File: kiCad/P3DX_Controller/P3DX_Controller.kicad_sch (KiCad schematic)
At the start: 19 parts, among them J1 Conn_01x10_Pin, J2 Conn_01x26_Pin, J3 Conn_01x10_Pin, J4 Conn_01x16_Pin, J5 Conn_01x03_Pin, J6 Conn_01x05_Pin, U1 TXS0108EPW, U3 ESP32-DevKitC

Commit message: 20251202
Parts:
- removed R5: DO NOT PLACE, Resistor_THT:R_Axial_DIN0204_L3.6mm_D1.6mm_P7.62mm_Horizontal, symbol Device:R
- removed U4: ~, p3dx:MPU6050, symbol p3dx:MPU6050
- added J6: Conn_01x03_Pin, Connector_PinHeader_2.54mm:PinHeader_1x03_P2.54mm_Vertical, symbol Connector:Conn_01x03_Pin
- added R4: DO NOT PLACE, Resistor_THT:R_Axial_DIN0204_L3.6mm_D1.6mm_P7.62mm_Horizontal, symbol Device:R
- renumbered C3 to C1, C4 to C2, J6 to J7, R4 to R1, R1 to R2, R2 to R5, U3 to U2, U2 to U3
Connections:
- net i2c-scl is gone; now on net L_ENCODER_A_LV: U2.36 (GPIO22)
- net i2c-sda is gone; now on net R_ENCODER_A_LV: U2.33 (GPIO21)
- net imu_int is gone; now on net lidar-motor: U2.12 (MTMS/GPIO14/ADC2_CH6)
- net rear_bumper is gone; now on net bumper: J3.1 (Pin_1), J3.2 (Pin_2), J3.3 (Pin_3), J3.4 (Pin_4), J3.5 (Pin_5), J3.6 (Pin_6), J3.7 (Pin_7), J3.8 (Pin_8), U2.8 (32K_XN/GPIO33/ADC1_CH5)
- net GND: now also J6.2 (Pin_2)
- net L_ENCODER_A_LV: no longer U2.17 (SD_DATA3/GPIO10)
- net L_ENCODER_B_LV: now also U2.25 (GPIO0/BOOT/ADC2_CH1); no longer U2.21 (SD_DATA0/GPIO7)
- net R_ENCODER_A_LV: no longer U2.16 (SD_DATA2/GPIO9)
- net R_ENCODER_B_LV: now also U2.24 (ADC2_CH2/GPIO2); no longer U2.22 (SD_DATA1/GPIO8)
- net R_MOTOR_DIR: now also U2.7 (32K_XP/GPIO32/ADC1_CH4); no longer U2.20 (SD_CLK/GPIO6)
- net VCC: now also J6.1 (Pin_1), R4.1
- net ucp_power_led: now also R4.2
- net front_bumper renamed bumper
- net bumper: no longer U2.7 (32K_XP/GPIO32/ADC1_CH4)

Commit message: 20251203
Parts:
- removed U2: ESP32-DevKitC, PCM_Espressif:ESP32-DevKitC, symbol PCM_Espressif:ESP32-DevKitC
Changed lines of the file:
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@@
 	)
 	(label "MOTOR_ENABLE"
-		(at 109.22 39.37 0)
+		(at 118.11 34.29 0)
 		(effects
 			(font
@@
 	)
 	(label "L_ENCODER_B_LV"
-		(at 109.22 34.29 0)
+		(at 118.11 29.21 0)
 		(effects
 			(font
@@
 	)
 	(label "R_ENCODER_B_LV"
-		(at 109.22 36.83 0)
+		(at 118.11 31.75 0)
 		(effects
 			(font
@@
 	)
 	(label "ucp_status_lv"
-		(at 43.18 46.99 180)
+		(at 34.29 53.34 180)
 		(effects
 			(font
@@
 	)
 	(label "R_MOTOR_PWM"
-		(at 109.22 62.23 0)
+		(at 118.11 57.15 0)
 		(effects
 			(font
@@
 		)
 	)
+	(label "ucp_power_led"
+		(at 38.1 166.37 0)
+		(effects
+			(font
+				(size 1.27 1.27)
+			)
+			(justify left bottom)
+		)
+	)
 	(label "R_ENCODER_B_LV"
 		(at 243.84 71.12 180)
@@
 	)
 	(label "R_ENCODER_A_LV"
-		(at 109.22 49.53 0)
+		(at 118.11 44.45 0)
 		(effects
 			(font
@@
 	)
 	(label "L_ENCODER_A_LV"
-		(at 109.22 52.07 0)
+		(at 118.11 46.99 0)
 		(effects
 			(font
@@
 	)
 	(label "V_BATTERY_MEASUREMENT"
-		(at 43.18 52.07 180)
+		(at 34.29 58.42 180)
 		(effects
 			(font
@@
 	)
 	(label "ucp_reset_lv"
-		(at 43.18 54.61 180)
+		(at 34.29 60.96 180)
 		(effects
 			(font
@@
 	)
 	(label "display_cs"
-		(at 109.22 41.91 0)
+		(at 118.11 36.83 0)
 		(effects
 			(font
@@
 	)
 	(label "bumper"
-		(at 43.18 34.29 180)
+		(at 34.29 40.64 180)
 		(effects
 			(font
@@
 	)
 	(label "lidar-tx"
-		(at 109.22 85.09 0)
+		(at 118.11 80.01 0)
 		(effects
 			(font
@@
 	)
 	(label "R_MOTOR_DIR"
-		(at 43.18 31.75 180)
+		(at 34.29 38.1 180)
 		(effects
 			(font
@@
 	)
 	(label "display_not_used"
-		(at 109.22 46.99 0)
+		(at 118.11 41.91 0)
 		(effects
 			(font
@@
 	)
 	(label "ucp_buzzer_pwm_lv"
-		(at 43.18 59.69 180)
+		(at 34.29 66.04 180)
 		(effects
 			(font
@@
 	)
 	(label "display_rst"
-		(at 43.18 41.91 180)
+		(at 34.29 48.26 180)
 		(effects
 			(font
@@
 	)
 	(label "lidar-motor"
-		(at 43.18 44.45 180)
+		(at 34.29 50.8 180)
 		(effects
 			(font
@@
 		)
 	)
+	(label "lidar-motor"
+		(at 124.46 107.95 0)
+		(effects
+			(font
+				(size 1.27 1.27)
+			)
+			(justify left bottom)
+		)
+	)
 	(label "bumper"
 		(at 182.88 97.79 0)
@@
 	)
 	(label "lidar-rx"
-		(at 109.22 87.63 0)
+		(at 118.11 82.55 0)
 		(effects
 			(font
@@
 	)
 	(label "display_RS_DC"
-		(at 43.18 39.37 180)
+		(at 34.29 45.72 180)
 		(effects
 			(font
@@
 	)
 	(label "display_clk"
-		(at 109.22 44.45 0)
+		(at 118.11 39.37 0)
 		(effects
 			(font
@@
 	)
 	(label "ucp_motors_lv"
-		(at 43.18 57.15 180)
+		(at 34.29 63.5 180)
 		(effects
 			(font
@@
 	)
 	(label "display_sda"
-		(at 109.22 54.61 0)
+		(at 118.11 49.53 0)
 		(effects
 			(font
@@
 	)
 	(label "L_MOTOR_PWM"
-		(at 109.22 57.15 0)
+		(at 118.11 52.07 0)
 		(effects
 			(font
@@
 	)
 	(label "L_MOTOR_DIR"
-		(at 109.22 59.69 0)
+		(at 118.11 54.61 0)
 		(effects
 			(font
@@
 	(symbol
 		(lib_id "power:GND")
-		(at 76.2 92.71 0)
+		(at 82.55 138.43 0)
 		(unit 1)
 		(exclude_from_sim no)
@@
 		(fields_autoplaced yes)
 		(property "Reference" "#PWR08"
-			(at 76.2 99.06 0)
+			(at 82.55 144.78 0)
 			(effects
 				(font
@@
 		)
 		(property "Value" "GND"
-			(at 76.2 97.79 0)
+			(at 82.55 143.51 0)
 			(effects
 				(font
@@
 		)
 		(property "Footprint" ""
-			(at 76.2 92.71 0)
+			(at 82.55 138.43 0)
 			(effects
 				(font
@@
 		)
 		(property "Datasheet" ""
-			(at 76.2 92.71 0)
+			(at 82.55 138.43 0)
 			(effects
 				(font
@@
 		)
 		(property "Description" "Power symbol creates a global label with name \"GND\" , ground"
-			(at 76.2 92.71 0)
+			(at 82.55 138.43 0)
 			(effects
 				(font
@@
 					(unit 1)
 				)
-			)
-		)
-	)
-	(symbol
-		(lib_id "PCM_Espressif:ESP32-DevKitC")
-		(at 76.2 57.15 0)
-		(unit 1)
-		(exclude_from_sim no)
-		(in_bom yes)
-		(on_board yes)
-		(dnp no)
-		(fields_autoplaced yes)
-		(property "Reference" "U2"
-			(at 78.3433 92.71 0)
-			(effects
-				(font
-					(size 1.27 1.27)
-				)
-				(justify left)
-			)
-		)
-		(property "Value" "ESP32-DevKitC"
-			(at 78.3433 95.25 0)
-			(effects
-				(font
-					(size 1.27 1.27)
-				)
-				(justify left)
-			)
-		)
-		(property "Footprint" "PCM_Espressif:ESP32-DevKitC"
-			(at 76.2 100.33 0)
-			(effects
-				(font
-					(size 1.27 1.27)
-				)
-				(hide yes)
-			)
-		)
-		(property "Datasheet" "https://docs.espressif.com/projects/esp-idf/zh_CN/latest/esp32/hw-reference/esp32/get-started-devkitc.html"
-			(at 76.2 102.87 0)
-			(effects
-				(font
-					(size 1.27 1.27)
-				)
-				(hide yes)
-			)
-		)
-		(property "Description" "Development Kit"
-			(at 76.2 57.15 0)
-			(effects
-				(font
-					(size 1.27 1.27)
-				)
-				(hide yes)
-			)
-		)
-		(pin "2"
-		)
-		(pin "7"
-		)
-		(pin "21"
-		)
-		(pin "37"
-		)
-		(pin "8"
-		)
-		(pin "19"
-		)
-		(pin "10"
-		)
-		(pin "6"
-		)
-		(pin "15"
-		)
-		(pin "34"
-		)
-		(pin "30"
-		)
-		(pin "1"
-		)
-		(pin "38"
-		)
-		(pin "26"
-		)
-		(pin "20"
-		)
-		(pin "12"
-		)
-		(pin "11"
-		)
-		(pin "25"
-		)
-		(pin "35"
-		)
-		(pin "32"
-		)
-		(pin "16"
-		)
-		(pin "23"
-		)
-		(pin "29"
-		)
-		(pin "22"
-		)
-		(pin "4"
-		)
-		(pin "14"
-		)
-		(pin "28"
-		)
-		(pin "5"
-		)
-		(pin "18"
-		)
-		(pin "17"
-		)
-		(pin "27"
-		)
-		(pin "31"
-		)
-		(pin "13"
-		)
-		(pin "9"
-		)
-		(pin "33"
-		)
-		(pin "36"
-		)
-		(pin "3"
-		)
-		(pin "24"
-		)
-		(instances
-			(project ""
-				(path "/ef99843a-7c8a-41b3-bbe8-92aaa291095d"
-					(reference "U2")
-					(unit 1)
-				)

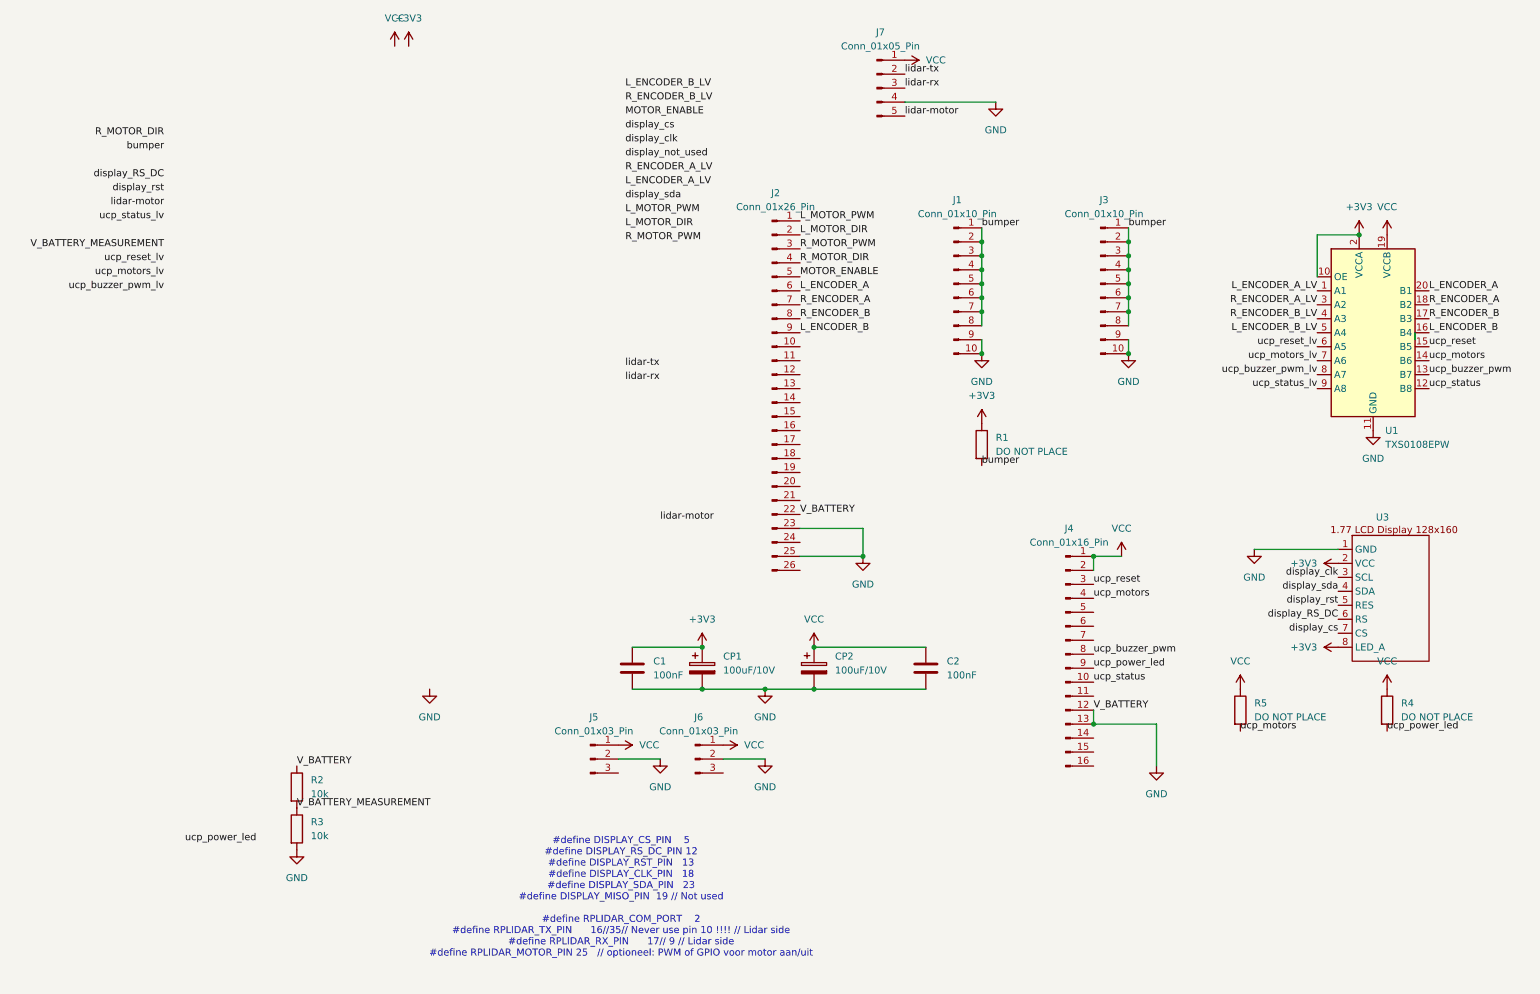
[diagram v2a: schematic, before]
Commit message: esp32-s3 change
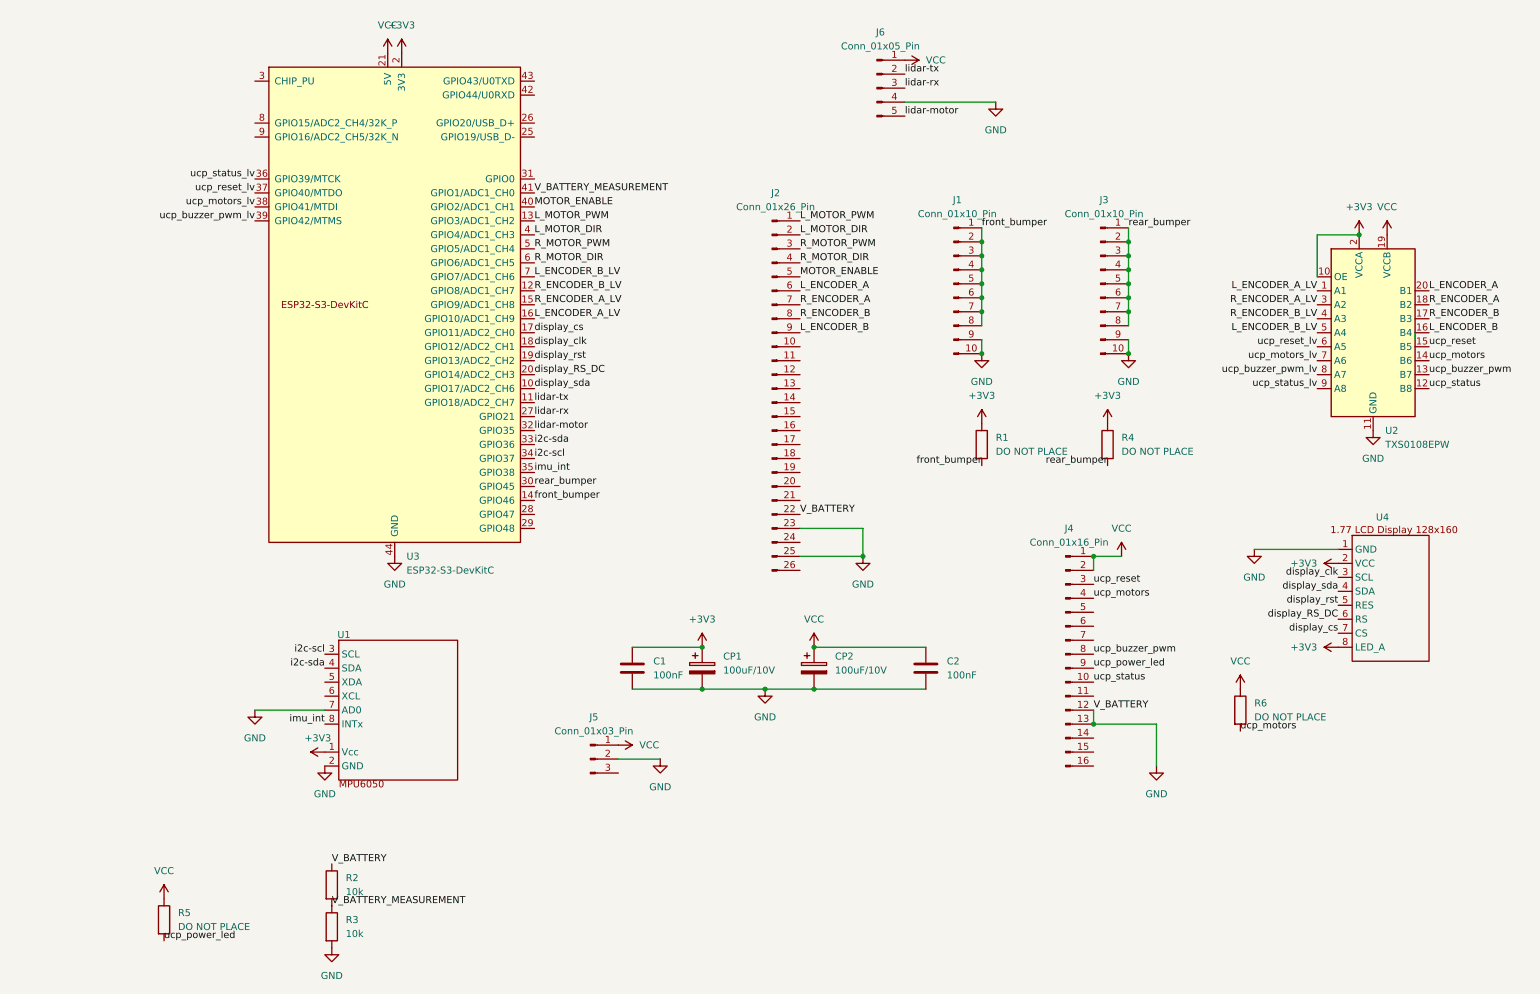
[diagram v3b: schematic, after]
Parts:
- removed J6: Conn_01x03_Pin, Connector_PinHeader_2.54mm:PinHeader_1x03_P2.54mm_Vertical, symbol Connector:Conn_01x03_Pin
- added R5: DO NOT PLACE, Resistor_THT:R_Axial_DIN0204_L3.6mm_D1.6mm_P7.62mm_Horizontal, symbol Device:R
- added U1: ~, p3dx:MPU6050, symbol p3dx:MPU6050
- added U3: ESP32-S3-DevKitC, PCM_Espressif:ESP32-S3-DevKitC, symbol PCM_Espressif:ESP32-S3-DevKitC
- renumbered J7 to J6, R5 to R6, U1 to U2, U3 to U4
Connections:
- net +3V3: now also R4.1, U1.1 (Vcc), U3.1 (3V3), U3.2 (3V3)
- net GND: now also U1.2 (GND), U1.7 (AD0), U3.22 (GND), U3.23 (GND), U3.24 (GND), U3.44 (GND)
- net L_ENCODER_A_LV: now also U3.16 (GPIO10/ADC1_CH9)
- net L_ENCODER_B_LV: now also U3.7 (GPIO7/ADC1_CH6)
- net L_MOTOR_DIR: now also U3.4 (GPIO4/ADC1_CH3)
- net L_MOTOR_PWM: now also U3.13 (GPIO3/ADC1_CH2)
- net MOTOR_ENABLE: now also U3.40 (GPIO2/ADC1_CH1)
- net R_ENCODER_A_LV: now also U3.15 (GPIO9/ADC1_CH8)
- net R_ENCODER_B_LV: now also U3.12 (GPIO8/ADC1_CH7)
- net R_MOTOR_DIR: now also U3.6 (GPIO6/ADC1_CH5)
- net R_MOTOR_PWM: now also U3.5 (GPIO5/ADC1_CH4)
- net VCC: now also R5.1, U3.21 (5V); no longer R4.1
- net V_BATTERY_MEASUREMENT: now also U3.41 (GPIO1/ADC1_CH0)
- net display_RS_DC: now also U3.20 (GPIO14/ADC2_CH3)
- net display_clk: now also U3.18 (GPIO12/ADC2_CH1)
- net display_cs: now also U3.17 (GPIO11/ADC2_CH0)
- net display_rst: now also U3.19 (GPIO13/ADC2_CH2)
- net display_sda: now also U3.10 (GPIO17/ADC2_CH6)
- net lidar-motor: now also U3.32 (GPIO35)
- net lidar-rx: now also U3.27 (GPIO21)
- net lidar-tx: now also U3.11 (GPIO18/ADC2_CH7)
- net ucp_buzzer_pwm_lv: now also U3.39 (GPIO42/MTMS)
- net ucp_motors_lv: now also U3.38 (GPIO41/MTDI)
- net ucp_power_led: now also R5.2; no longer R4.2
- net ucp_reset_lv: now also U3.37 (GPIO40/MTDO)
- net ucp_status_lv: now also U3.36 (GPIO39/MTCK)
- net bumper renamed front_bumper
- net front_bumper: now also U3.14 (GPIO46); no longer J3.1 (Pin_1), J3.2 (Pin_2), J3.3 (Pin_3), J3.4 (Pin_4), J3.5 (Pin_5), J3.6 (Pin_6), J3.7 (Pin_7), J3.8 (Pin_8)
- new net i2c-scl: U1.3 (SCL), U3.34 (GPIO37)
- new net i2c-sda: U1.4 (SDA), U3.33 (GPIO36)
- new net imu_int: U1.8 (INTx), U3.35 (GPIO38)
- new net rear_bumper: J3.1 (Pin_1), J3.2 (Pin_2), J3.3 (Pin_3), J3.4 (Pin_4), J3.5 (Pin_5), J3.6 (Pin_6), J3.7 (Pin_7), J3.8 (Pin_8), R4.2, U3.30 (GPIO45)
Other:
- note removed: "#define DISPLAY_CS_PIN 5 #define DISPLAY_RS_DC_PIN 12 #define DISPLAY_RST_PIN 13 #define DISPLAY_CLK_PIN 18 #define DISPLAY_SDA_PIN 23 #define DISPLAY_MISO_PIN 19 // Not used #define RPLIDAR_COM_PORT 2 #define RPLIDAR_TX_PIN 16//35// Never use pin 10 !!!! // Lidar side #define RPLIDAR_RX_PIN 17// 9 // Lidar side #define RPLIDAR_MOTOR_PIN 25 // optioneel: PWM of GPIO voor motor aan/uit"
- company: (none) -> Avans Hogeschool
- title: (none) -> Pioneer 3dx Mobile Robot Controller
- moved on the sheet: R2, R3

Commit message: 20251204
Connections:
- net GND: no longer J2.22 (Pin_22), J4.12 (Pin_12), R2.1
- net L_ENCODER_B: now also J2.12 (Pin_12); no longer J2.9 (Pin_9)
- net R_ENCODER_A: now also J2.8 (Pin_8); no longer J2.7 (Pin_7)
- net R_ENCODER_B: now also J2.10 (Pin_10); no longer J2.8 (Pin_8)
- net V_BATTERY: now reaches J4.11 (Pin_11)
- net V_BATTERY: now also J2.22 (Pin_22), R2.1
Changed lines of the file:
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@@
-	)
-	(junction
-		(at 203.2 144.78)
-		(diameter 0)
-		(color 0 0 0 0)
 	)
 	(junction
@@
 		(pts
 			(xy 203.2 114.3) (xy 208.28 114.3)
-		)
-		(stroke
-			(width 0)
-			(type default)
-		)
-	)
-	(wire
-		(pts
-			(xy 203.2 142.24) (xy 203.2 144.78)
 		)
 		(stroke
@@
 	)
 	(label "V_BATTERY"
-		(at 203.2 142.24 0)
+		(at 203.2 139.7 0)
 		(effects
 			(font
@@
 	)
 	(label "R_ENCODER_B"
-		(at 149.86 71.12 0)
+		(at 149.86 76.2 0)
 		(effects
 			(font
@@
 	)
 	(label "L_ENCODER_B"
-		(at 149.86 73.66 0)
+		(at 149.86 81.28 0)
 		(effects
 			(font
@@
 	)
 	(label "R_ENCODER_A"
-		(at 149.86 68.58 0)
-		(effects
-			(font
+		(at 149.86 71.12 0)
+		(effects
+			(font
